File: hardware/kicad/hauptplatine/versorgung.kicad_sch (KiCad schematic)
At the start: 33 parts, among them J201 Solar 1, J202 Solar 2, U201 BQ25185DLHR, U202 RT9080-33GJ5, U203 TPS22917DBV, U204 TPS70933DBV

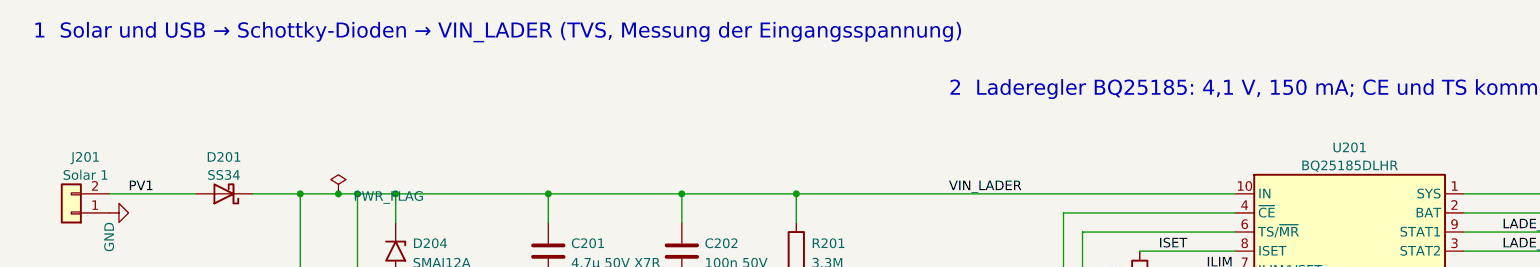
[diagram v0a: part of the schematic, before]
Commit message: HW-09: USB-C-Buchse entfaellt, Laden ueber zwei Pads J301 (Entscheidung Philipp)
J301 jetzt Conn_01x02 DNP (1 GND, 2 +5 V -> D203), R303/R304 entfernt; anschluesse.md J9 neu,
netz_tests.py prueft J9 gegen das Dokument, VBUS nur Pad 2 + D203, kein U302/R303/R304/R307/R308;
pin_footprint.py ohne USB. Dokumente: mcu-funk.md 1.3, Lastenheft K5/M5/M8, Pflichtenheft 4,
Fiverr (177 Teile), Entscheidungsregister HW-09 (Teilentscheid getroffen), Befundregister HW26-20,
CHANGELOG, KiCad-README (Stueckliste 177), Bericht (Nachtrag).
pruefen.sh: reproduzierbar, ERC 0, Netzpruefung 220/220, Pin/Footprint 177/0.

Co-Authored-By: Claude Fable 5.1 <noreply@anthropic.com>
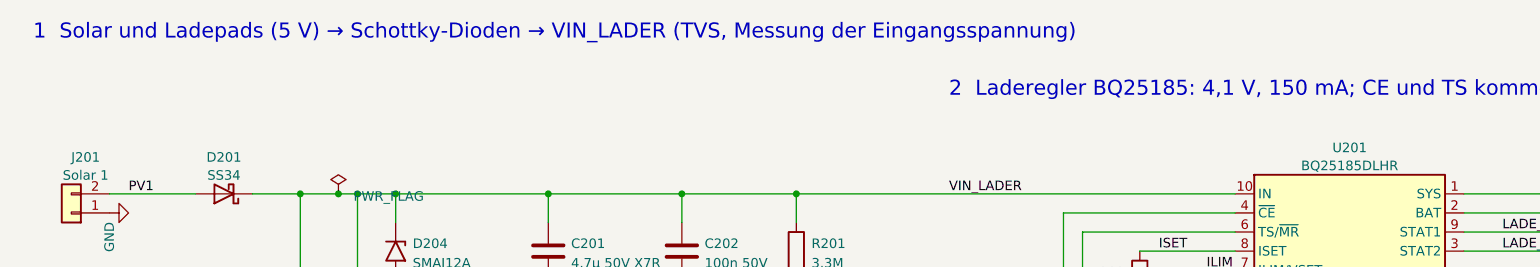
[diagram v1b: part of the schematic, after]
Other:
- note added: "1 Solar und Ladepads (5 V) → Schottky-Dioden → VIN_LADER (TVS, Messung der Eingangsspannung)"
- note removed: "1 Solar und USB → Schottky-Dioden → VIN_LADER (TVS, Messung der Eingangsspannung)"
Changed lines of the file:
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@@
 		(comment 3 "Umgebung [A]: Gehäuse −20 … +60 °C, Betauung möglich; VIN ≤ 12 V dauernd, 25 V absolut")
+	)
+	(text "1  Solar und Ladepads (5 V) → Schottky-Dioden → VIN_LADER (TVS, Messung der Eingangsspannung)"
+		(exclude_from_sim no)
+		(at 30.48 55.88 0)
+		(effects
+			(font
+				(size 2 2)
+			)
+			(justify left bottom)
+		)
 	)
 	(text "4  SYS → 3,3 V (RT9080) → geschaltete Sensorschiene 3V3_SW (TPS22917, Ein/Aus von der MCU)"
@@
 		(exclude_from_sim no)
 		(at 152.4 63.5 0)
-		(effects
-			(font
-				(size 2 2)
-			)
-			(justify left bottom)
-		)
-	)
-	(text "1  Solar und USB → Schottky-Dioden → VIN_LADER (TVS, Messung der Eingangsspannung)"
-		(exclude_from_sim no)
-		(at 30.48 55.88 0)
 		(effects
 			(font
@@
 			)
 		)
-		(property "Description" "USB lädt, speist nie ins Panel"
+		(property "Description" "Ladepads J301 (5 V, HW-09): lädt, speist nie ins Panel, sperrt Verpolung"
 			(at 55.88 116.84 0)
 			(hide yes)
